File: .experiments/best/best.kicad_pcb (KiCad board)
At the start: 2 copper layers, 140 x 90 mm, 39 parts, among them J1 USB_C, J2 Output, J3 Debug, Q1 FS8205A, U1 USBLC6-2SC6, U2 BQ24072, U3 HY2113-KB5B, U4 MT3608, U5 AP2112K-3.3, U6 LN61CN3302MR-G

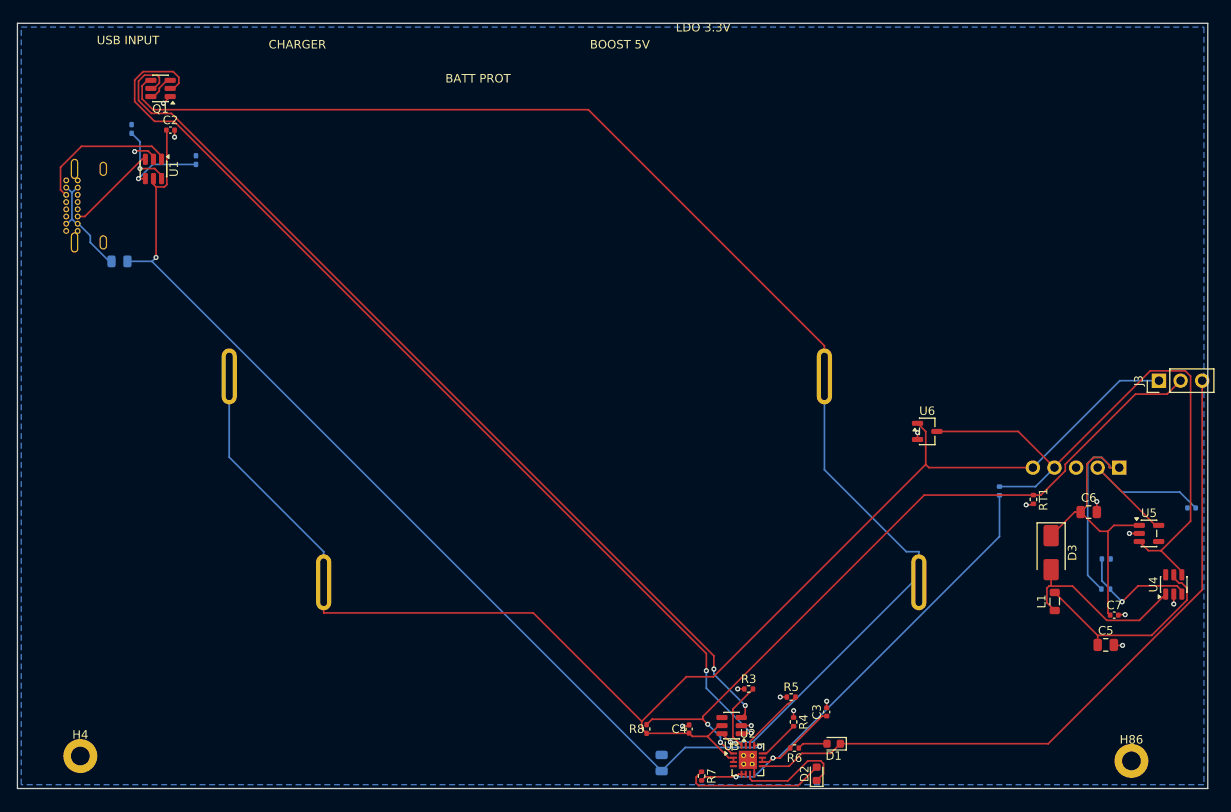
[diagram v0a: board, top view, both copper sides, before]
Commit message: fix: rotation convention (CW), layer flip pad mirroring, hard pad-containment gate
- Fix _update_pad_positions to use KiCad's rotation convention
  (x'=x*cos+y*sin, y'=-x*sin+y*cos) instead of CCW math convention
- Fix _best_rotation_for_edge: delta = current - desired (not desired - current)
- Fix _optimize_rotations and _place_clusters early rotation to use CW formula
- Mirror pad X offsets in _assign_layers when flipping components to B.Cu
  to match KiCad Flip() behavior
- Reorder solve(): assign layers BEFORE edge pinning so pinned positions
  account for flipped pad geometry
- Add _clamp_pads_to_board after _restore_pinned_positions (defense in depth)
- Add hard pads_outside_board gate in pipeline: reject placement if ANY
  pad is outside the board boundary (zero tolerance)
- Add pads_outside_board count to PlacementEngine return dict

Score: 92.1, 26/26 nets routed, 0 pads outside board (verified by KiCad)
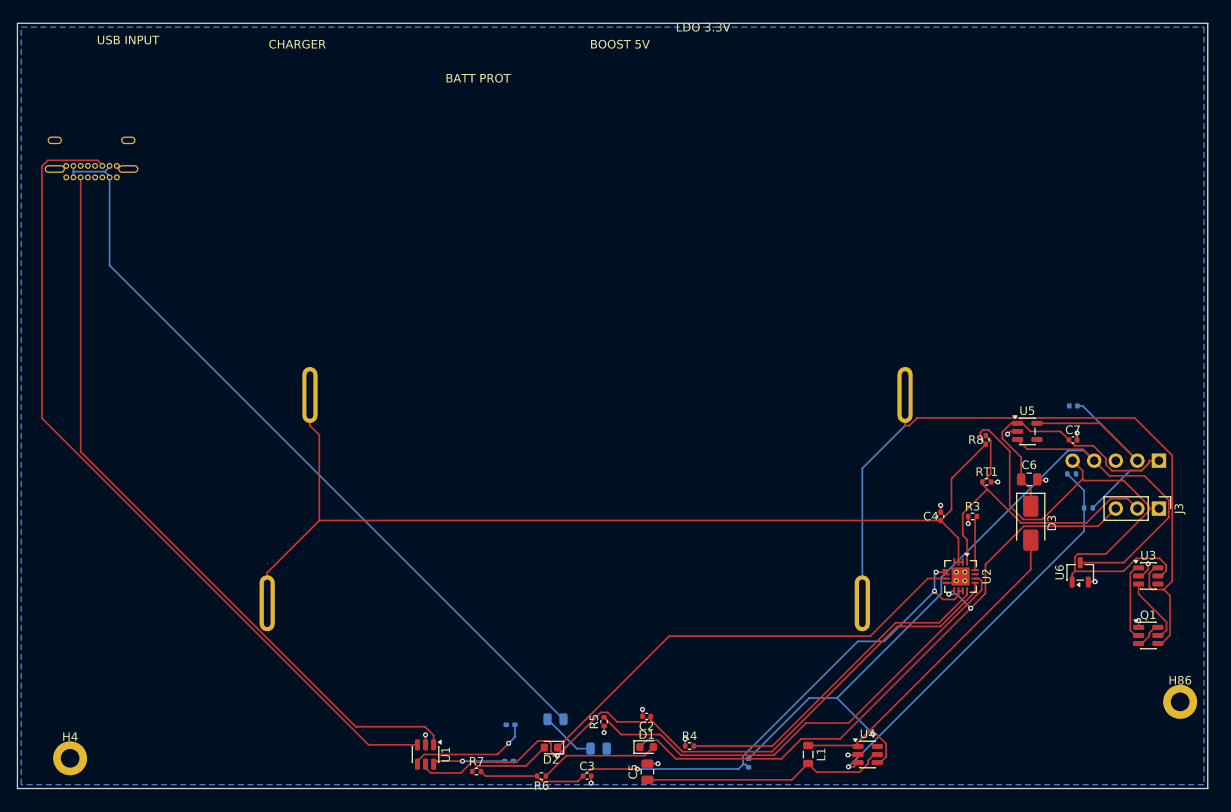
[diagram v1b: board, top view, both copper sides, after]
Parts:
- moved Q1 132.8 mm to (133.0, 72.0), turned to 0 degrees
- moved C2 88.8 mm to (74.0, 81.5), turned to 180 degrees
- moved R1 86.6 mm to (57.8, 86.8), turned to 0 degrees
- moved R2 76.0 mm to (58.0, 82.5), turned to 180 degrees
- moved U1 75.9 mm to (48.0, 86.0)
- moved F1 74.4 mm to (63.3, 81.9), turned to 0 degrees
- moved C5 55.9 mm to (74.1, 88.0), turned to 90 degrees
- moved R8 52.4 mm to (113.9, 49.0)
- moved U3 52.1 mm to (133.0, 65.0), turned to 0 degrees
- moved R11 43.5 mm to (86.0, 87.0)
- moved U4 41.2 mm to (100.0, 86.0), turned to 0 degrees
- moved C4 38.7 mm to (108.6, 58.0)
- moved L1 34.1 mm to (93.0, 86.0), turned to -90 degrees
- moved R3 33.2 mm to (112.3, 58.0)
- moved U2 33.0 mm to (110.9, 65.1), turned to -90 degrees
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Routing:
- net Net-(Q1A-G): track 117.2 -> 9.17 mm, vias 2 -> 0
- net Net-(Q1B-G): track 110.8 -> 8.04 mm, vias 2 -> 0
- net Net-(J1-CC2): track 10.7 -> 97.4 mm
- net Net-(F1-Pad2): track 13.0 -> 92.7 mm
- net Net-(J1-CC1): track 17.3 -> 88.7 mm
- net /CELL_NEG: track 160.1 -> 92.2 mm, vias 1 -> 0
- net Net-(U2-TMR): track 7.97 -> 56.2 mm
- net /NTC_SENSE: track 85.8 -> 38.1 mm, vias 2 -> 0
- net Net-(D2-K): track 12.7 -> 53.9 mm
- net Net-(U2-ILIM): track 5.01 -> 40.0 mm
- net Net-(U4-FB): track 14.5 -> 48.1 mm
- net /EN: track 72.9 -> 103.5 mm, vias 0 -> 1
- net /VBUS: track 119.0 -> 90.7 mm, vias 2 -> 1
- net Net-(D3-A): track 22.0 -> 38.5 mm
- net /5V: track 53.6 -> 42.6 mm
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
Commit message: fix: connector orientation using body center instead of footprint origin
_best_rotation_for_edge() measured pad centroid from footprint origin,
which for connectors like USB-C is at a corner pad. The centroid angle
(~22°) snapped to 0° delta, leaving the connector facing wrong.

Fix: add body_center (courtyard bbox center) to Component data model
and use it as reference. From body center, pad centroid is at 270°
(perpendicular to opening), correctly producing rotation 270° for
left-edge connectors.

Also rewrote orientation_check.py to validate facing dynamically
using body-center-to-pad-centroid angle instead of hard-coded rotation
table.
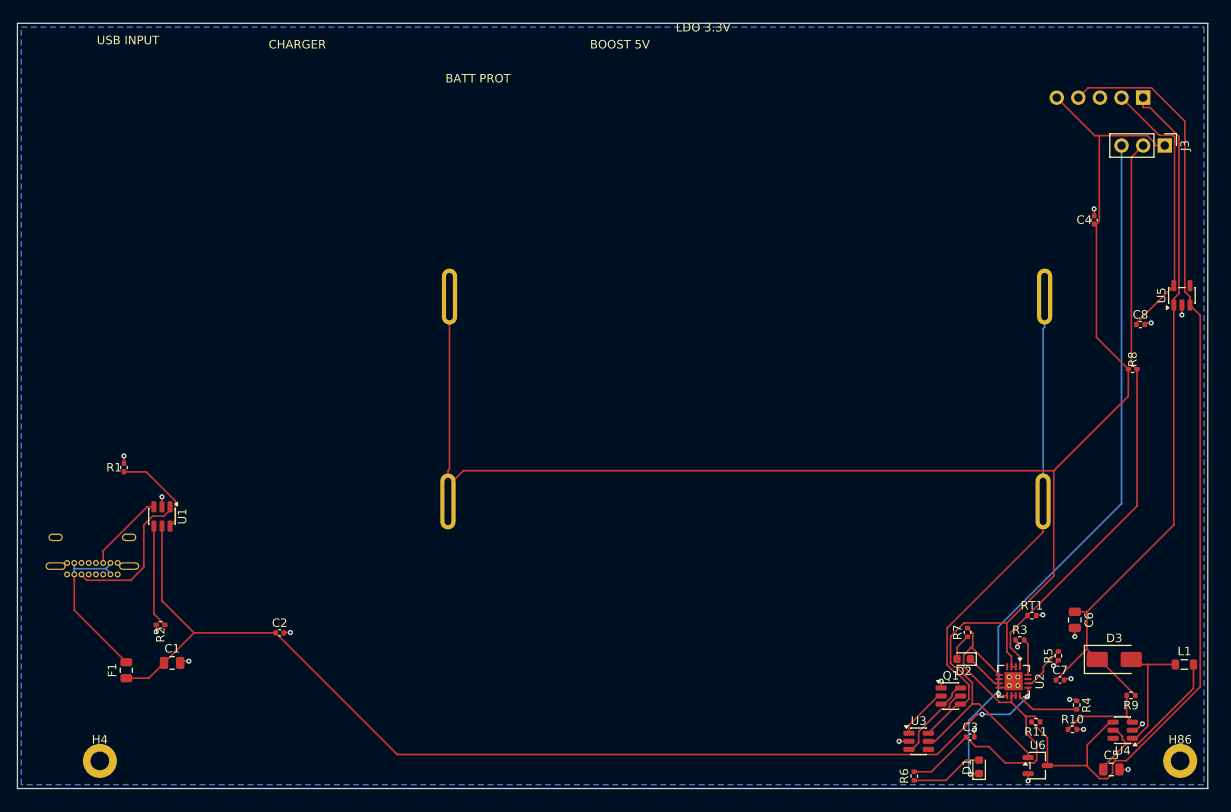
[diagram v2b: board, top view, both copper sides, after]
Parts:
- C1, C8, F1, R1, R10, R11, R2, R9: moved to F.Cu
- moved R7 60.0 mm to (111.7, 71.6), turned to 90 degrees
- moved R1 57.0 mm to (12.5, 52.2), turned to 90 degrees
- moved C5 54.6 mm to (128.7, 87.8), turned to 0 degrees
- moved R5 54.0 mm to (122.4, 74.4)
- moved C1 51.2 mm to (18.2, 75.2)
- moved F1 50.8 mm to (12.8, 76.1), turned to 90 degrees
- moved D2 49.6 mm to (111.3, 74.8)
- moved J1 46.7 mm to (5.84, 64.8)
- moved R4 45.8 mm to (124.6, 80.2), turned to -90 degrees
- moved L1 45.5 mm to (137.3, 75.4), turned to 0 degrees
- moved C3 45.3 mm to (112.1, 83.9)
- moved C2 44.3 mm to (30.8, 71.7), turned to 0 degrees
- moved R6 43.8 mm to (105.5, 88.5), turned to 90 degrees
- moved R2 42.8 mm to (16.8, 70.8)
- moved J2 42.7 mm to (132.4, 8.75)
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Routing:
- net Net-(J1-CC2): track 97.4 -> 9.54 mm
- net Net-(F1-Pad2): track 92.7 -> 19.7 mm
- net Net-(J1-CC1): track 88.7 -> 17.5 mm
- net Net-(U2-TMR): track 56.2 -> 5.49 mm
- net Net-(D2-K): track 53.9 -> 4.57 mm
- net /5V: track 42.6 -> 86.1 mm
- net /VBUS: track 90.7 -> 132.1 mm, vias 1 -> 2
- net Net-(U4-FB): track 48.1 -> 10.9 mm, vias 1 -> 0
- net Net-(U2-ILIM): track 40.0 -> 7.41 mm
- net /CELL_NEG: track 92.2 -> 59.7 mm
- net /VBAT: track 183.0 -> 215.3 mm
- net /NTC_SENSE: track 38.1 -> 68.8 mm
- net /VSYS: track 72.9 -> 46.5 mm, vias 3 -> 0
- net Net-(D3-A): track 38.5 -> 15.1 mm
- net /EN: track 103.5 -> 118.2 mm, vias 1 -> 0
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
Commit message: fix: edge connector 180° rotation error on B.Cu (back layer)
When THT connectors are flipped to B.Cu by _assign_layers(), KiCad's
Flip() mirrors the local X-axis. _best_rotation_for_edge() was using
F.Cu outward direction assumptions regardless of layer, causing the
USB connector opening to face inward (toward the board) instead of
outward.

Fix: swap left/right outward angles when comp.layer == Layer.BACK.

Also fix unrelated UnboundLocalError for stop_mid_batch in single-worker
experiment mode.
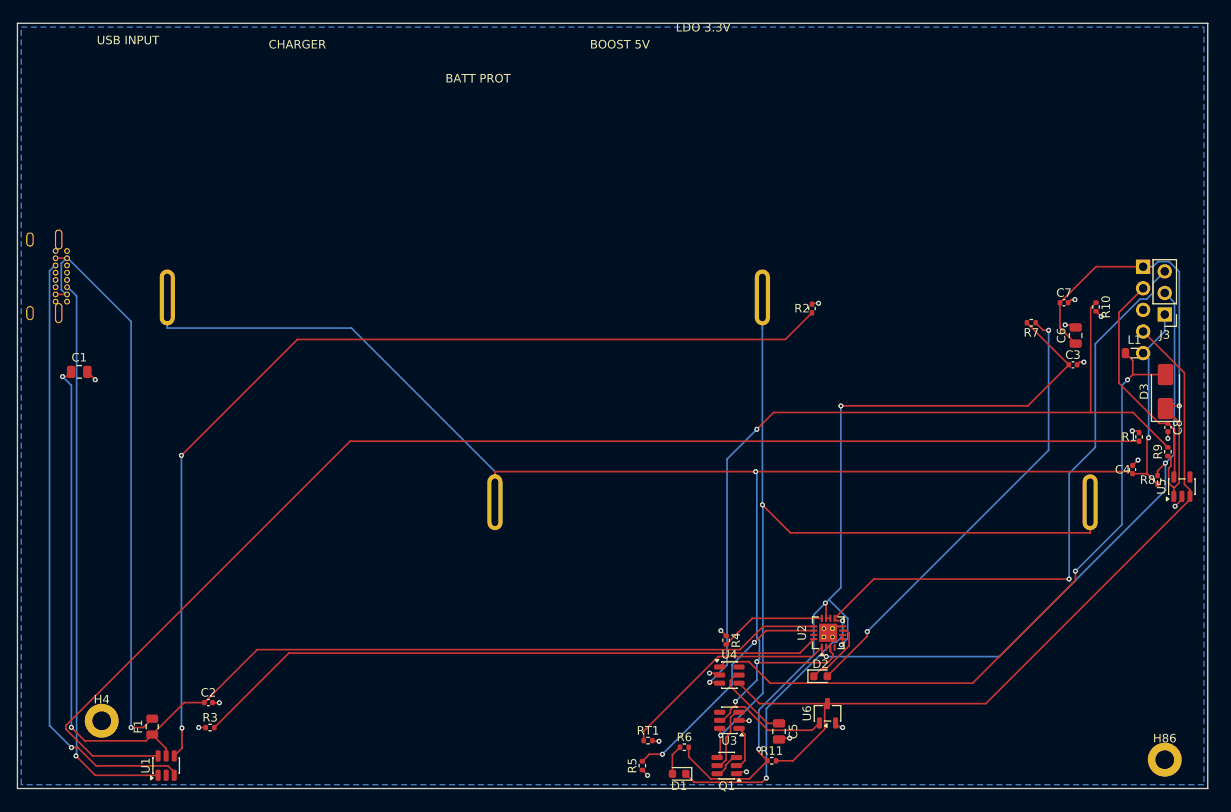
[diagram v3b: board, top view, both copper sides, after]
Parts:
- moved R1 119.4 mm to (131.9, 48.6)
- moved R3 95.8 mm to (22.7, 82.8)
- moved R2 85.2 mm to (93.4, 33.5), turned to 90 degrees
- moved R5 50.6 mm to (73.5, 87.3)
- moved R10 49.8 mm to (126.9, 33.4), turned to -90 degrees
- moved RT1 47.5 mm to (74.2, 84.4)
- moved U4 46.7 mm to (83.7, 76.7), turned to 0 degrees
- moved C3 45.4 mm to (124.1, 40.2)
- moved C7 44.4 mm to (123.1, 32.9)
- moved R4 41.9 mm to (83.4, 72.6)
- moved C5 39.3 mm to (89.6, 83.3), turned to -90 degrees
- moved R7 37.2 mm to (119.2, 35.2), turned to 180 degrees
- moved L1 37.1 mm to (131.4, 38.8)
- moved C1 35.9 mm to (7.27, 41.0)
- moved D1 35.3 mm to (77.8, 88.3), turned to 180 degrees
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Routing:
- net Net-(R1-Pad1): track 10.7 -> 152.6 mm
- net Net-(R2-Pad1): track 12.1 -> 116.9 mm, vias 0 -> 2
- net Net-(U4-FB): track 10.9 -> 97.3 mm, vias 0 -> 2
- net Net-(U2-ISET): track 4.30 -> 74.8 mm
- net Net-(D3-A): track 15.1 -> 81.9 mm, vias 0 -> 2
- net Net-(J1-CC2): track 9.54 -> 71.8 mm, vias 0 -> 1
- net /VSYS: track 46.5 -> 104.4 mm, vias 0 -> 4
- net Net-(D2-A): track 3.14 -> 53.4 mm, vias 0 -> 2
- net Net-(F1-Pad2): track 19.7 -> 68.9 mm, vias 0 -> 1
- net Net-(J1-CC1): track 17.5 -> 66.3 mm, vias 0 -> 1
- net /CELL_NEG: track 59.7 -> 100.8 mm, vias 0 -> 2
- net /NTC_SENSE: track 68.8 -> 101.5 mm, vias 0 -> 2
- net /5V: track 86.1 -> 55.2 mm, vias 0 -> 1
- net Net-(U2-TMR): track 5.49 -> 27.9 mm, vias 0 -> 2
- net /EN: track 118.2 -> 96.3 mm
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
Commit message: feat: hierarchical group-based placement with SMT-opposite-THT scoring
Add two-phase placement strategy: intra-group placement keeps
functionally related components together, then inter-group arrangement
positions groups on the board respecting signal flow order.

Key changes:
- New group_placer.py and groups.py for functional group discovery
  and hierarchical placement
- SMT-opposite-THT and group_coherence scoring metrics (types.py)
- bbox now uses body_center for accurate overlap detection
- GUI toggles for new placement features and stale process cleanup
- Pipeline supports hierarchical mode with flat fallback
- Retuned scoring weights for new metrics
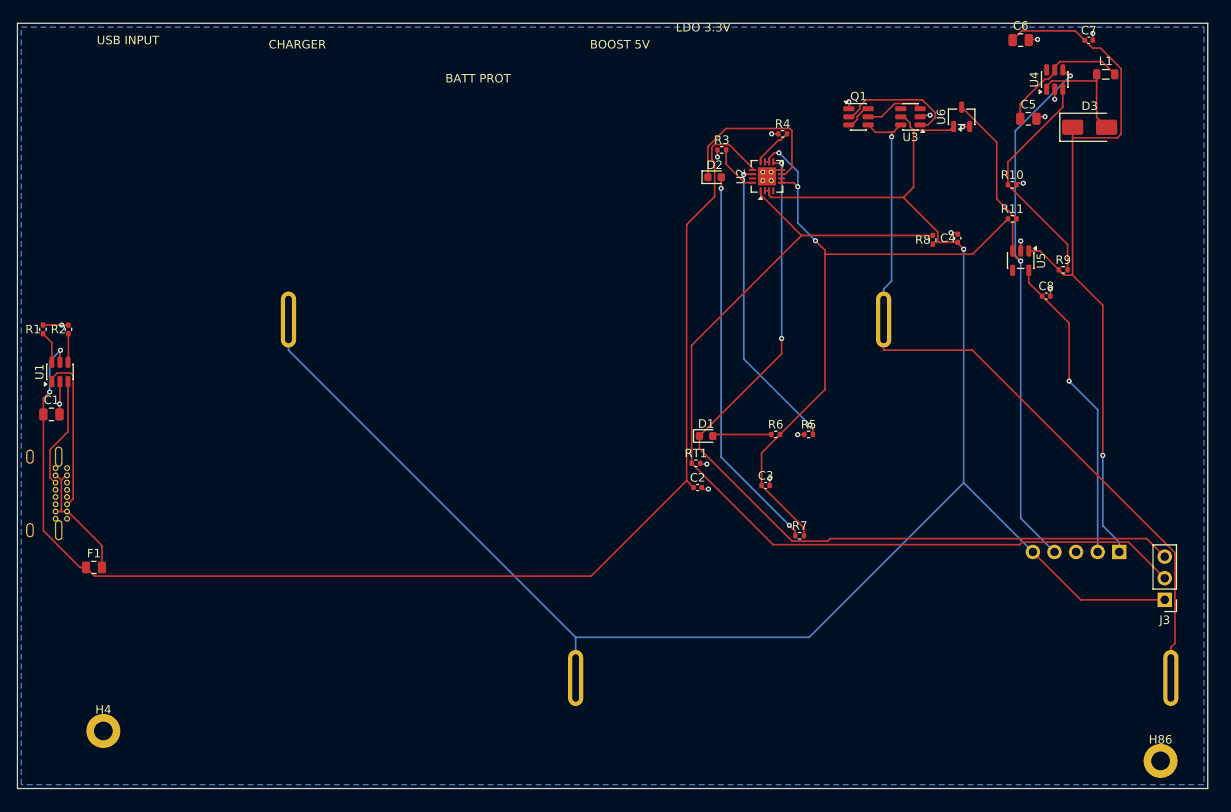
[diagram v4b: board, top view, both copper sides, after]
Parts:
- moved R1 129.5 mm to (3.00, 36.0)
- moved R3 90.8 mm to (82.8, 14.9)
- moved R2 87.5 mm to (6.00, 36.0)
- moved U4 79.8 mm to (122.0, 6.61), turned to 90 degrees
- moved Q1 77.9 mm to (98.9, 11.0), turned to 0 degrees
- moved C5 77.8 mm to (118.9, 11.2), turned to 0 degrees
- moved U3 74.1 mm to (105.0, 11.0)
- moved U6 71.9 mm to (111.1, 11.0)
- moved R11 69.7 mm to (117.0, 23.0)
- moved C2 62.9 mm to (80.0, 54.6)
- moved D2 60.0 mm to (82.0, 18.1)
- moved R4 59.9 mm to (90.0, 13.0), turned to 0 degrees
- moved U2 54.2 mm to (88.2, 18.0)
- moved U1 48.0 mm to (5.00, 41.0)
- moved R5 43.6 mm to (93.1, 48.4), turned to 0 degrees
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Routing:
- net Net-(R1-Pad1): track 152.6 -> 3.79 mm
- net Net-(R2-Pad1): track 116.9 -> 3.37 mm, vias 2 -> 0
- net Net-(U4-FB): track 97.3 -> 26.8 mm, vias 2 -> 0
- net Net-(U2-ISET): track 74.8 -> 5.68 mm
- net Net-(D3-A): track 81.9 -> 13.2 mm, vias 2 -> 0
- net Net-(J1-CC2): track 71.8 -> 13.1 mm, vias 1 -> 0
- net Net-(F1-Pad2): track 68.9 -> 15.2 mm, vias 1 -> 0
- net Net-(J1-CC1): track 66.3 -> 18.8 mm, vias 1 -> 0
- net /5V: track 55.2 -> 87.2 mm
- net /VSYS: track 104.4 -> 80.7 mm, vias 4 -> 3
- net /NTC_SENSE: track 101.5 -> 116.3 mm, vias 2 -> 0
- net /VBUS: track 139.7 -> 154.1 mm
- net /EN: track 96.3 -> 83.2 mm, vias 0 -> 2
- net Net-(D2-K): track 8.01 -> 20.4 mm
- net /CELL_NEG: track 100.8 -> 89.6 mm, vias 2 -> 1
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
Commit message: chore: remove generated reports, stale experiment data, and old Flask dashboard
Remove 17 tracked files that are either generated outputs (reports,
dashboards, PNGs, GIFs), stale experiment data from old runs, SQLite
runtime artifacts, or root-level duplicates.

Removed:
- report.html, .experiments/report.html (regenerated each run)
- .experiments/*.png, *.gif (regenerated each run)
- .experiments/baseline_*, post_*, test_fixes* (stale data)
- .experiments/llups.db-shm, llups.db-wal (runtime artifacts)
- dashboard_app.py (superseded by gui/ package)
- LLUPS_best.kicad_pcb (duplicate of .experiments/best/best.kicad_pcb)
- BOM.csv (keeping BOM.xlsx)

Updated .gitignore to prevent re-tracking of generated artifacts.
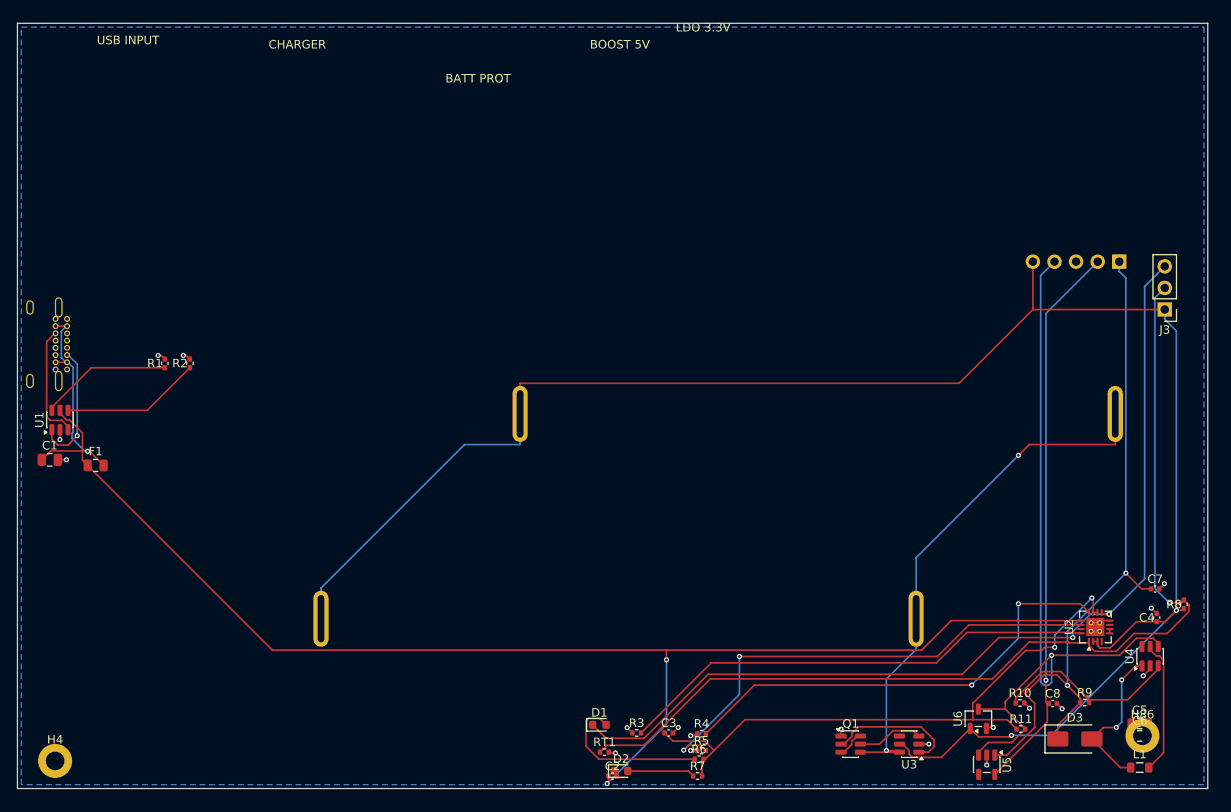
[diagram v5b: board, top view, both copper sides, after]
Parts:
- moved C6 82.9 mm to (132.0, 83.7)
- moved L1 81.6 mm to (132.0, 87.5)
- moved Q1 73.8 mm to (98.0, 84.8)
- moved U3 73.8 mm to (104.9, 84.8)
- moved C5 72.4 mm to (132.0, 82.5)
- moved D3 72.0 mm to (124.4, 84.2)
- moved R4 71.2 mm to (80.5, 83.6)
- moved U6 70.8 mm to (113.0, 81.8)
- moved D2 70.7 mm to (71.0, 87.9)
- moved R3 69.3 mm to (72.8, 83.5)
- moved U4 68.7 mm to (133.2, 74.4)
- moved U2 65.6 mm to (126.8, 71.0)
- moved C7 65.0 mm to (133.8, 66.5)
- moved R10 60.9 mm to (117.9, 79.9)
- moved R11 60.0 mm to (118.0, 83.0)
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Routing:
- net Net-(U2-ISET): track 5.68 -> 56.7 mm
- net Net-(U2-ILIM): track 4.73 -> 54.2 mm, vias 0 -> 2
- net Net-(D2-A): track 45.8 -> 7.95 mm, vias 2 -> 0
- net /3V3: track 36.5 -> 65.6 mm
- net /CELL_NEG: track 89.6 -> 62.9 mm, vias 1 -> 2
- net Net-(U2-TMR): track 35.0 -> 58.5 mm
- net Net-(D2-K): track 20.4 -> 0.00 mm
- net /CHG_N: track 98.8 -> 112.4 mm
- net Net-(R2-Pad1): track 3.37 -> 16.4 mm
- net Net-(D1-A): track 6.96 -> 19.2 mm
- net Net-(R1-Pad1): track 3.79 -> 15.6 mm
- net /VSYS: track 80.7 -> 72.6 mm, vias 3 -> 2
- net /EN: track 83.2 -> 90.9 mm, vias 2 -> 1
- net /VBAT: track 209.9 -> 216.8 mm, vias 1 -> 2
- net Net-(F1-Pad2): track 15.2 -> 22.0 mm, vias 0 -> 1
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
